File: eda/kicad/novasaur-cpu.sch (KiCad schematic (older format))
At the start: 29 parts, among them U14 27C020, U15 AS6C4008, U16 74F574, U17 74F163, U18 74F163, U19 74F541, U20 74F574, U21 74F574, U22 74F257, U23 74F574, U24 74F574, U25 74F574, U26 74F574, U27 74F244, U27 74F541

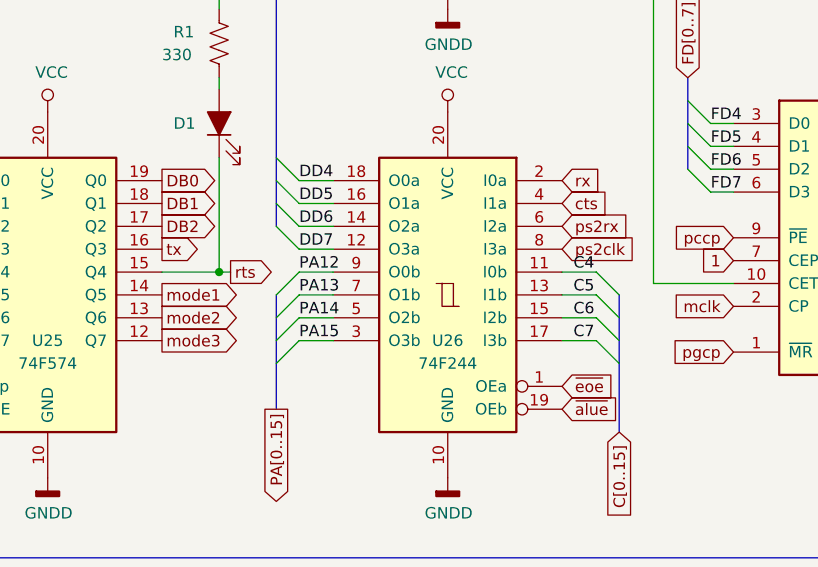
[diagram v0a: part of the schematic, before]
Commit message: add dedicated ps2 clock enable line Use mode0|1 to select VDAC using DRL
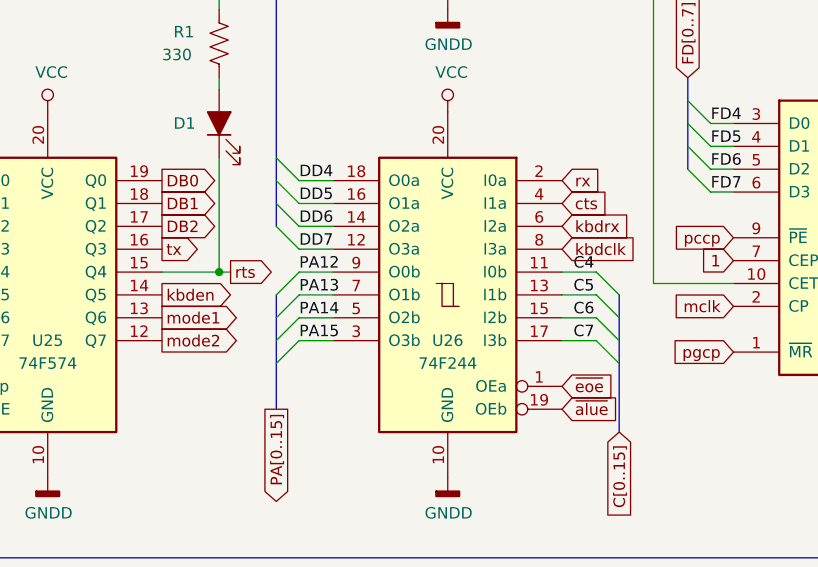
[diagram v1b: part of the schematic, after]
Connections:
- net mode3 is gone; now on net mode2: U23.12 (Q7)
- net mode1: now also U23.13 (Q6); no longer U23.14 (Q5)
- net mode2: no longer U23.13 (Q6)
- net ps2clk renamed kbdclk
- net ps2rx renamed kbdrx
- new net kbden: U23.14 (Q5)
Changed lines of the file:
@@
 Sheet 2 4
 Title "Central Processing Unit"
-Date "2020-07-18"
+Date "2020-08-20"
 Rev "1.7"
 Comp ""
@@
 Text GLabel 2350 6450 2    50   Output ~ 0
 rts
-Text GLabel 2050 6550 2    50   Output ~ 0
+Text GLabel 2050 6650 2    50   Output ~ 0
 mode1
-Text GLabel 2050 6650 2    50   Output ~ 0
-mode2
 Text GLabel 2050 6050 2    50   Output ~ 0
 DB0
@@
 DB2
 Text GLabel 2050 6750 2    50   Output ~ 0
-mode3
+mode2
 Wire Wire Line
 	2300 5300 2300 5250
@@
 cts
 Text GLabel 3800 6350 2    50   Input ~ 0
-ps2clk
+kbdclk
 Text GLabel 3800 6250 2    50   Input ~ 0
-ps2rx
+kbdrx
 Entry Bus Bus
 	5700 900  5800 800
@@
 Text GLabel 3950 1300 1    50   BiDi ~ 0
 DD[0..7]
+Text GLabel 2050 6550 2    50   Output ~ 0
+kbden
 Wire Bus Line
 	850  800  10150 800

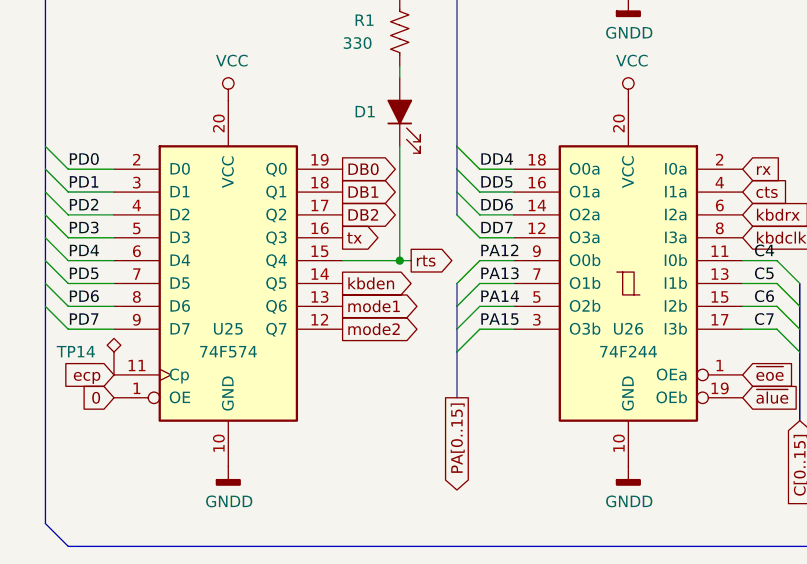
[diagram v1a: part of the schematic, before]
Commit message: refactor comms Add keyboard scan jump page, overload tx mode state to select keyboard jump page
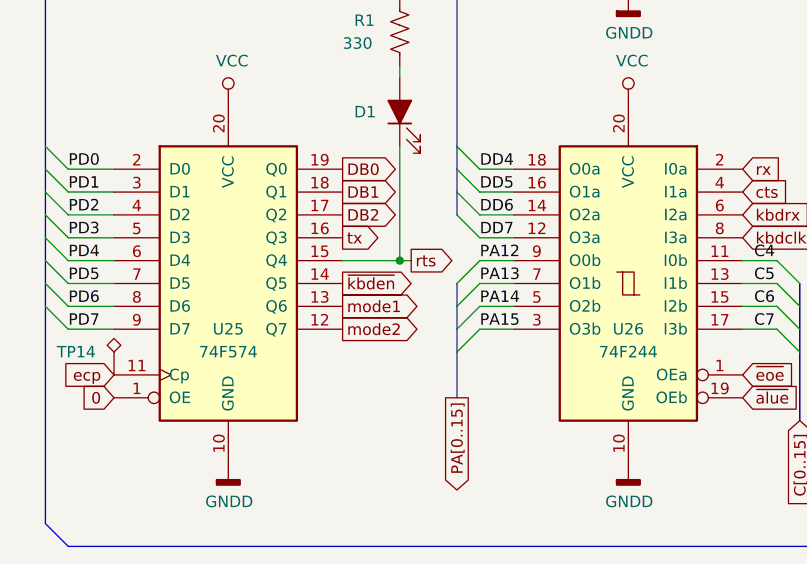
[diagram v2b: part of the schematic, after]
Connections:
- net kbden renamed ~kbden
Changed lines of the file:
@@
 DD[0..7]
 Text GLabel 2050 6550 2    50   Output ~ 0
-kbden
+~kbden
 Wire Bus Line
 	850  800  10150 800

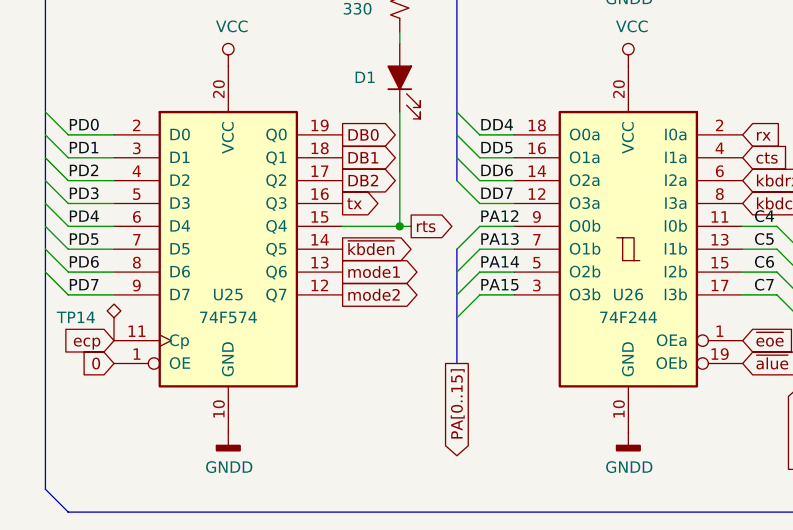
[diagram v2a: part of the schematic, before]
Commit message: fix video timing debug and finish video modes
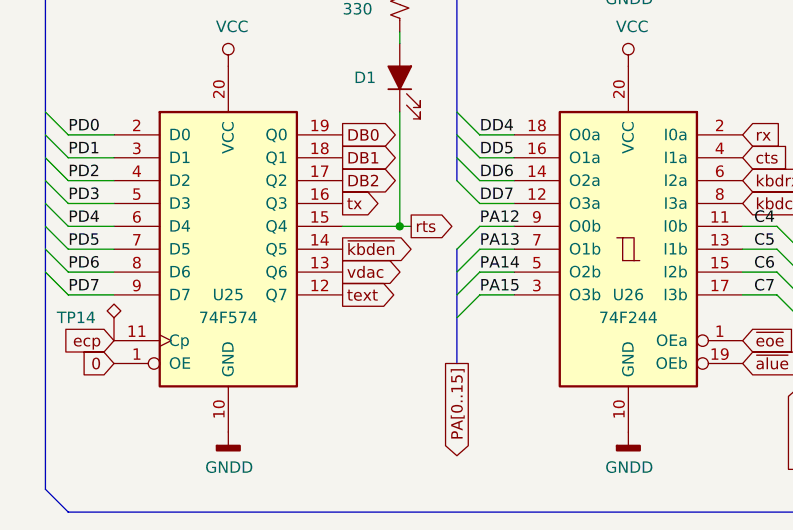
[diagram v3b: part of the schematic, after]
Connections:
- net mode1 renamed vdac
- net mode2 renamed text
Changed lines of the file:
@@
 Sheet 2 4
 Title "Central Processing Unit"
-Date "2020-08-20"
+Date "2020-09-10"
 Rev "1.7"
 Comp ""
@@
 rts
 Text GLabel 2050 6650 2    50   Output ~ 0
-mode1
+vdac
 Text GLabel 2050 6050 2    50   Output ~ 0
 DB0
@@
 DB2
 Text GLabel 2050 6750 2    50   Output ~ 0
-mode2
+text
 Wire Wire Line
 	2300 5300 2300 5250
